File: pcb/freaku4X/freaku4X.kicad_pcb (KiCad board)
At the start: 2 copper layers, 190.5 x 95.2 mm, 97 parts, among them SW1 RotaryEncoder_Switch, SW10 SW_SPST, SW11 SW_SPST, SW12 SW_SPST, SW13 SW_SPST, SW14 SW_SPST, SW15 SW_SPST, SW16 SW_SPST, SW17 SW_SPST, SW18 SW_SPST, SW19 SW_SPST, SW2 SW_SPST, SW20 SW_SPST, SW21 SW_SPST, SW22 SW_SPST, SW23 SW_SPST, SW24 SW_SPST, SW25 SW_SPST, SW26 SW_SPST, SW27 SW_SPST, SW28 SW_SPST, SW29 SW_SPST, SW3 SW_SPST, SW30 SW_SPST, SW31 SW_SPST, SW32 SW_SPST, SW33 SW_SPST, SW34 SW_SPST, SW35 SW_SPST, SW36 SW_SPST, SW37 SW_SPST, SW38 SW_SPST, SW39 SW_SPST, SW4 SW_SPST, SW40 SW_SPST, SW41 SW_SPST, SW42 SW_SPST, SW43 SW_SPST, SW44 SW_SPST, SW5 SW_SPST, SW6 SW_SPST, SW7 SW_SPST, SW8 SW_SPST, SW9 SW_SPST, U1 ProMicro

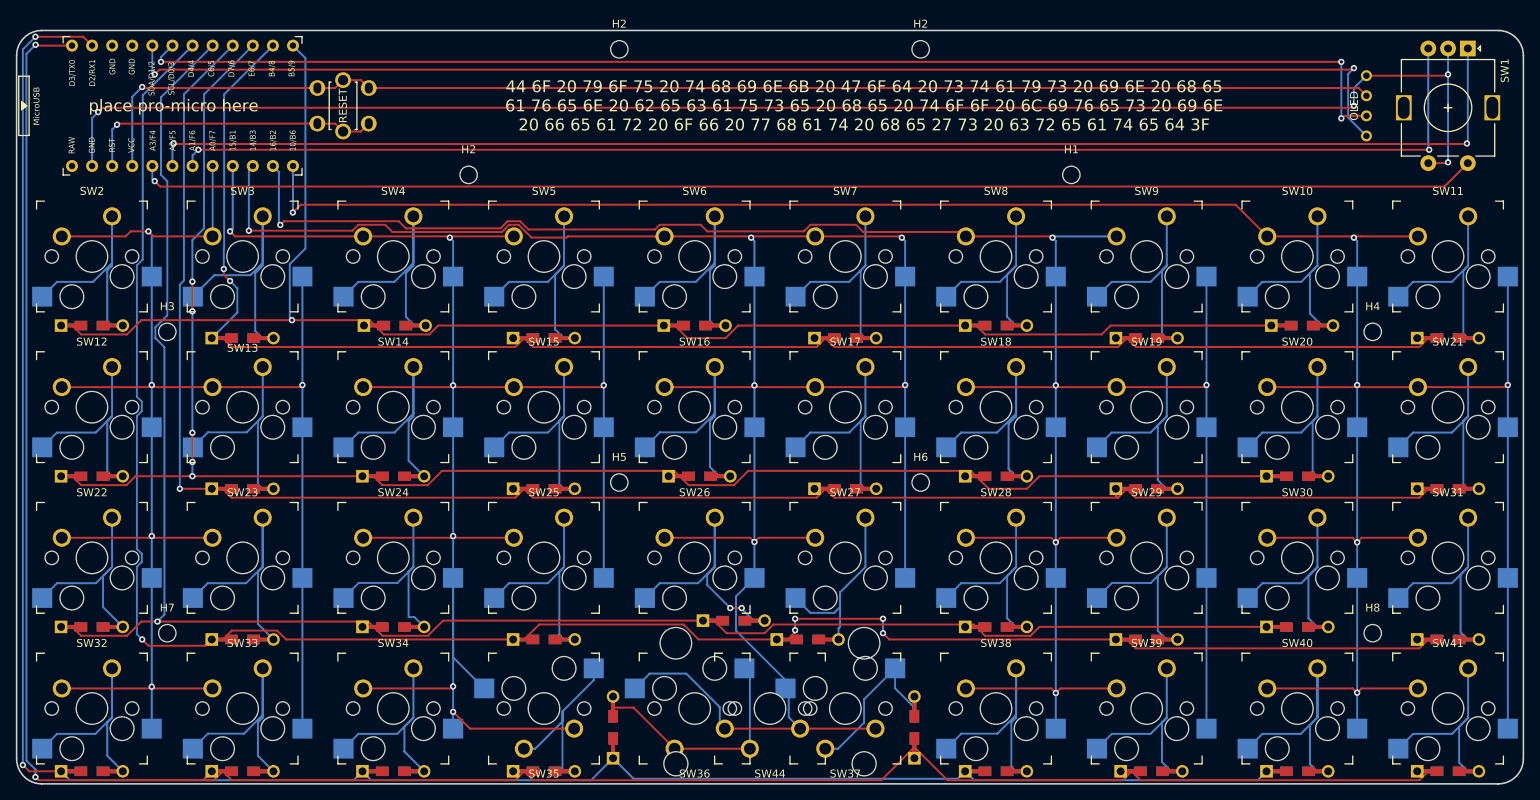
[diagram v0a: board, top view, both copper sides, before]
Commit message: Add Battery and Switch for Nice!Nano
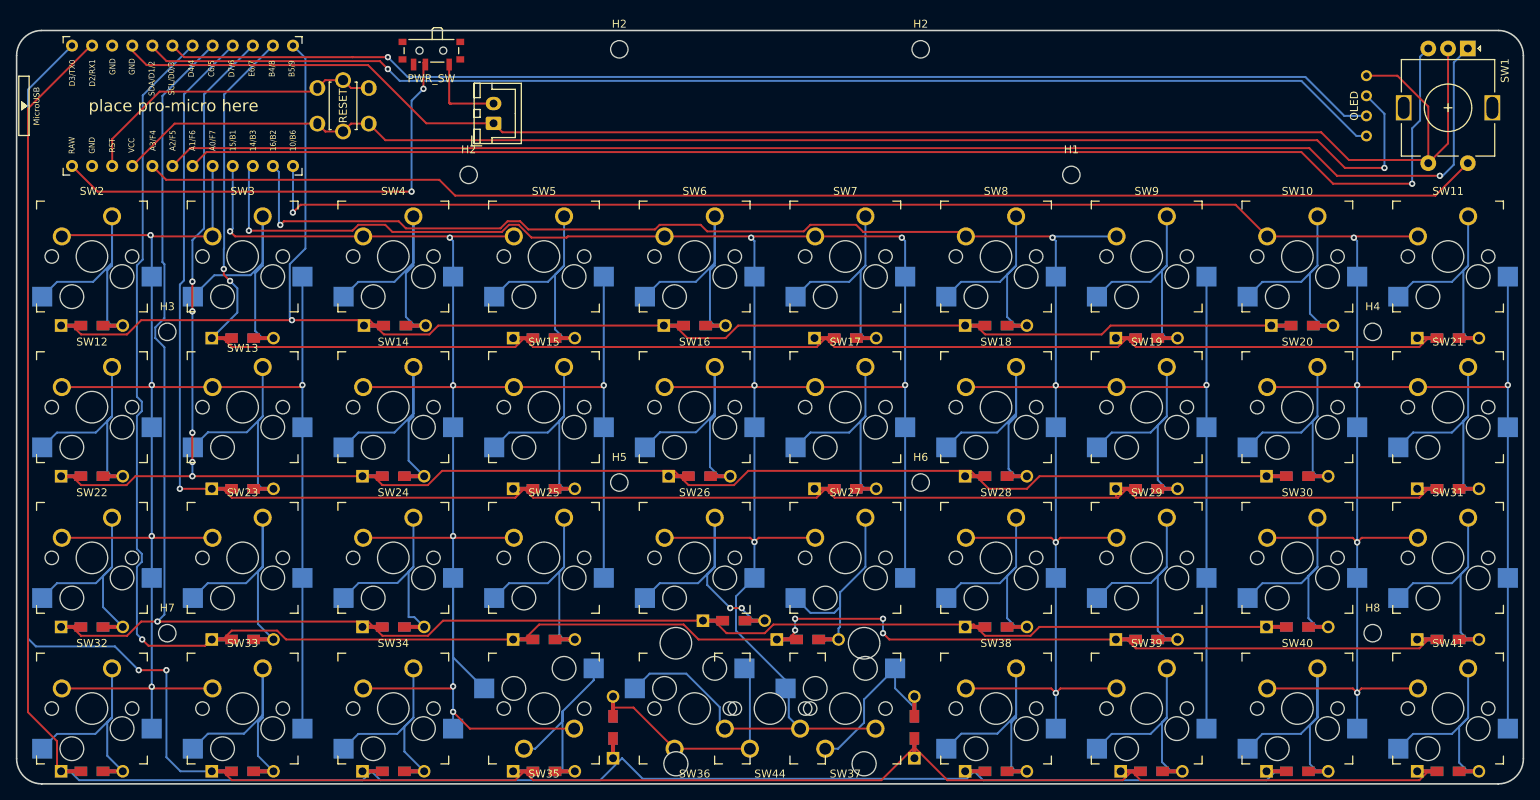
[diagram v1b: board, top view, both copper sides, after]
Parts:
- added ?: , clipboard:a534e012-eb56-4867-9d9e-b51b9e9253d1, F.Cu at (119.8, 53.9)
- added PWR_SW: SW_SPDT_PCM12, Button_Switch_SMD:SW_SPDT_PCM12, F.Cu at (108.0, 50.5)
- turned SW42 to 0 degrees
- turned SW43 to -90 degrees
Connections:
- U1 pad 24: unconnected-(U1-Pad24) -> raw
- U1 pad 3: unconnected-(U1-Pad3) -> gnd
- U1 pad 4: unconnected-(U1-Pad4) -> gnd
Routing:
- net raw: track 0.00 -> 61.9 mm, vias 0 -> 2
- net battery: track 0.00 -> 11.0 mm
- net row8: track 282.8 -> 272.6 mm
- net row7: track 262.9 -> 254.1 mm, vias 2 -> 0
- net sda: track 165.5 -> 157.7 mm, vias 2 -> 1
- net scl: track 162.3 -> 154.7 mm, vias 3 -> 1
- net vcc: track 166.6 -> 173.9 mm
- net padB: track 170.8 -> 174.5 mm, vias 2 -> 1
- net padA: track 178.5 -> 180.4 mm, vias 2 -> 1
- net gnd: track 201.7 -> 203.3 mm, vias 4 -> 0
- net rst: track 38.2 -> 39.7 mm, vias 1 -> 0
- net col1: track 217.9 -> 216.9 mm
- net encoder_switch: vias 1 -> 0
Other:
- board text removed: "44 6F 20 79 6F 75 20 74 68 69 6E 6B 20 47 6F 64 20 73 74 61 79 73 20 69 6E 20 68 65 61 76 65 6E 20 62 65 63 61 75 73 65 20 68 65 20 74 6F 6F 20 6C 69 76 65 73 20 69 6E 20 66 65 61 72 20 6F 66 20 77 68 61 74 20 68 65 27 73 20 63 72 65 61 74 65 64 3F"
- board text removed: "by sporewoh"
- board text removed: "freaku4X v0.1"
- board text removed: "{dblquote}You cheated not only the game, but yourself. You didn't grow. You didn't improve. You took a shortcut and gained nothing. You experienced a hollow victory. Nothing was risked and nothing was gained. It's sad you don't know the difference.{dblquote} - Sun Tzu"
